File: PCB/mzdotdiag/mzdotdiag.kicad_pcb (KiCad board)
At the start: 2 copper layers, 58 parts, among them J1 Conn_01x25, J2 RST, J3 BOOT, J4 UART, Q1 Q_NPN_BEC, Q2 Q_NPN_BEC, Q3 Q_NPN_BEC, Q4 Q_NPN_BEC, Q5 Q_NPN_BEC, Q6 Q_NPN_BEC, Q7 Q_NPN_BEC, Q8 Q_NPN_BEC, Q9 Q_NPN_BEC, SW1 SW_Push, U1 4050, U3 ESP32-WROOM-32

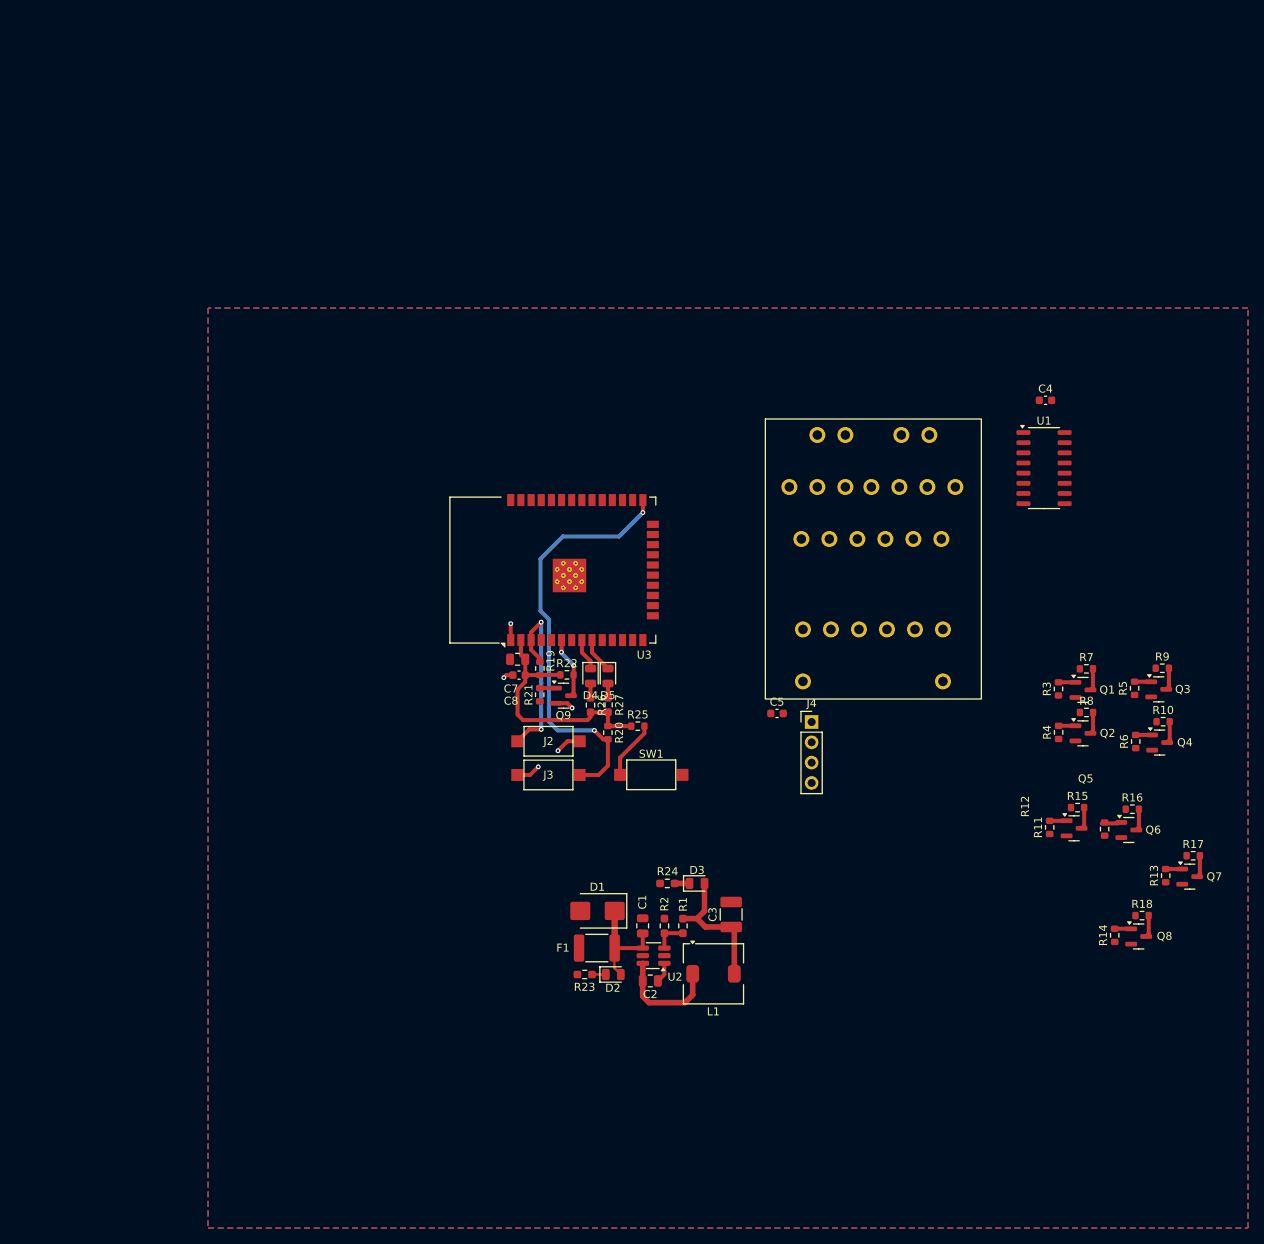
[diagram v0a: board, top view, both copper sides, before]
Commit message: schematic and pcb update with new levelshifter IC
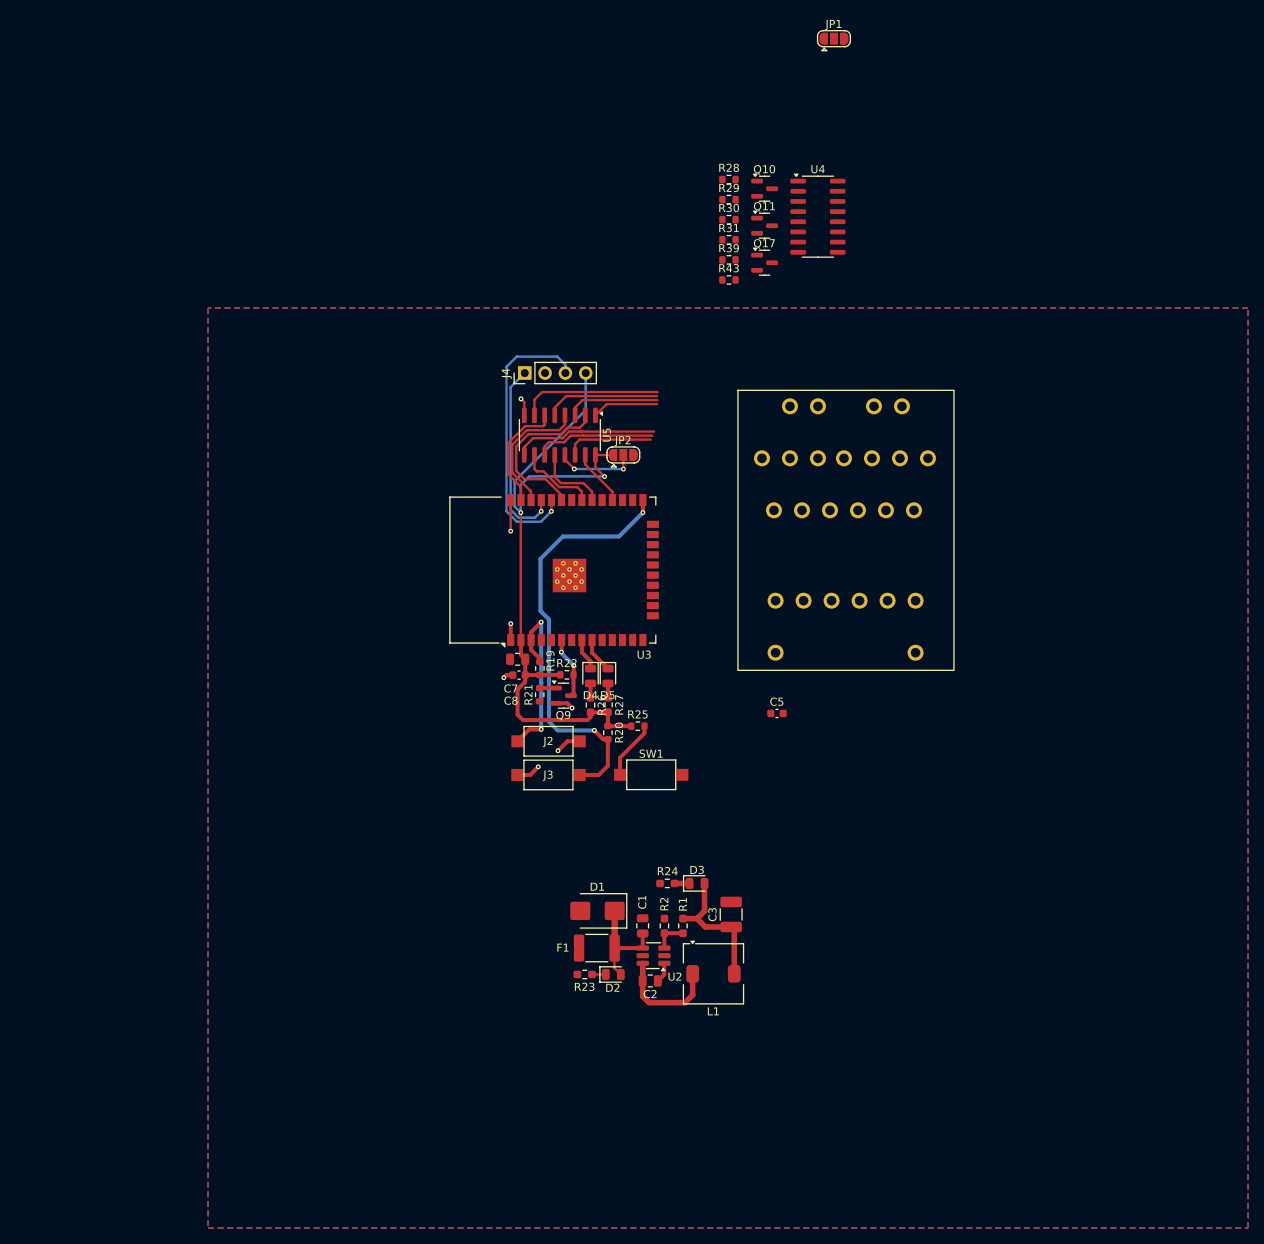
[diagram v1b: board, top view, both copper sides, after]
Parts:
- removed C4: 100nF, Capacitor_SMD:C_0603_1608Metric
- removed Q1, Q2, Q3, Q4, Q5, Q6, Q7, Q8: Q_NPN_BEC, Package_TO_SOT_SMD:SOT-23
- removed R10, R15, R16, R17, R18, R7, R8, R9: 10k, Resistor_SMD:R_0603_1608Metric
- removed R11, R12, R13, R14, R3, R4, R5, R6: 1k, Resistor_SMD:R_0603_1608Metric
- removed U1: 4050, Package_SO:SO-16_3.9x9.9mm_P1.27mm
- added JP1: SolderJumper_3_Open, Jumper:SolderJumper-3_P1.3mm_Open_RoundedPad1.0x1.5mm, F.Cu at (128.2, 6.33)
- added JP2: SolderJumper_3_Open, Jumper:SolderJumper-3_P1.3mm_Open_RoundedPad1.0x1.5mm, F.Cu at (101.9, 58.4)
- added Q10: Q_NPN_BEC, Package_TO_SOT_SMD:SOT-23, F.Cu at (119.6, 25.1)
- added Q11: Q_NPN_BEC, Package_TO_SOT_SMD:SOT-23, F.Cu at (119.6, 29.7)
- added Q17: Q_NPN_BEC, Package_TO_SOT_SMD:SOT-23, F.Cu at (119.6, 34.3)
- added R28: 1k, Resistor_SMD:R_0603_1608Metric, F.Cu at (115.1, 23.9)
- added R29: 10k, Resistor_SMD:R_0603_1608Metric, F.Cu at (115.1, 26.4)
- added R30: 1k, Resistor_SMD:R_0603_1608Metric, F.Cu at (115.1, 29.0)
- added R31: 10k, Resistor_SMD:R_0603_1608Metric, F.Cu at (115.1, 31.5)
- added R39: 1k, Resistor_SMD:R_0603_1608Metric, F.Cu at (115.1, 34.0)
- added R43: 10k, Resistor_SMD:R_0603_1608Metric, F.Cu at (115.1, 36.5)
- added U4: MC14504B, Package_SO:SOIC-16_3.9x9.9mm_P1.27mm, F.Cu at (126.2, 28.6)
- added U5: MC14504B, Package_SO:SOIC-16_3.9x9.9mm_P1.27mm, F.Cu at (94.0, 55.9)
- moved J4 56.5 mm to (89.6, 48.1), turned to 90 degrees
- moved J1 4.96 mm to (129.5, 65.3)
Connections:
- U3 pad 10: /FAC3V3 -> unconnected-(U3-IO25-Pad10)
- U3 pad 11: /FAB3V3 -> unconnected-(U3-IO26-Pad11)
- U3 pad 12: /FSC3V3 -> unconnected-(U3-IO27-Pad12)
- U3 pad 13: /ESP32_TFA -> /ESP32_TAT
- U3 pad 14: /ESP32_TAT -> /ESP32_TFA
- U3 pad 28: /ESP32_TAC -> /FSC3V3
- U3 pad 30: /ESP32_TEN -> /FAB3V3
- U3 pad 31: /ESP32_TSC -> /FAC3V3
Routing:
- net /3.3V: track 48.7 -> 105.9 mm, vias 0 -> 2
- net Net-(J4-Pin_3): track 0.00 -> 35.5 mm, vias 0 -> 1
- net Net-(J4-Pin_1): track 0.00 -> 23.8 mm, vias 0 -> 1
- net /FEN3V3: track 0.00 -> 21.4 mm
- net /FAC: track 0.00 -> 18.0 mm
- net /FAT: track 0.00 -> 17.7 mm
- net /FBS3V3: track 0.00 -> 16.7 mm
- net /FAB: track 0.00 -> 15.1 mm
- net /FAT3V3: track 0.00 -> 14.5 mm
- net /FBS: track 0.00 -> 14.4 mm
- net /FEN: track 0.00 -> 11.6 mm
- net /FSC: track 0.00 -> 11.0 mm
- net Net-(JP2-C): track 0.00 -> 10.2 mm, vias 0 -> 2
- net /FAC3V3: track 0.00 -> 9.90 mm
- net /FAB3V3: track 0.00 -> 9.22 mm
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
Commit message: updates to PCB
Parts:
- moved JP1 34.5 mm to (138.7, 39.2)
- moved U4 31.6 mm to (114.9, 58.1), turned to 90 degrees
- moved R1 29.6 mm to (128.4, 94.6)
- moved R2 29.6 mm to (126.1, 94.6)
- moved R24 29.6 mm to (126.4, 89.3)
- moved D3 29.6 mm to (130.1, 89.3)
- moved L1 29.6 mm to (132.2, 100.6)
- moved U2 29.6 mm to (124.7, 98.3)
- moved C3 29.6 mm to (134.4, 93.2)
- moved D2 29.6 mm to (119.7, 100.7)
- moved F1 29.6 mm to (117.6, 97.4)
- moved C1 29.6 mm to (123.3, 94.6)
- moved C2 29.6 mm to (124.3, 101.5)
- moved D1 29.6 mm to (117.7, 92.7)
- moved R23 29.6 mm to (116.1, 100.7)
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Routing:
- net /3.3V: track 105.9 -> 171.1 mm
- net Net-(U3-IO5): track 7.34 -> 38.4 mm
- net /B+: track 8.31 -> 21.8 mm, vias 0 -> 2
- net GND: track 18.0 -> 20.1 mm, vias 7 -> 8
- net /FSC: track 11.0 -> 13.1 mm
- net /FAB: track 15.1 -> 16.9 mm
- net /FAC: track 18.0 -> 19.6 mm
- net Net-(J3-Pin_2): track 53.2 -> 52.1 mm
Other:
- board text added: "BOOT"
- board text added: "BTN1"
- board text added: "RST"

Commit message: pcb upd
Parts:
- moved J1 10.6 mm to (143.5, 64.6)
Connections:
- U3 pad 14: /ESP32_TFA -> /ESP32_TAB
- U3 pad 16: /ESP32_TBS -> /ESP32_TSC
- U3 pad 23: /ESP32_TAB -> /ESP32_TEN
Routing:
- net /ESP32_TAB: track 0.00 -> 30.9 mm
- net /ESP32_TSC: track 0.00 -> 23.9 mm
- net /TEN: track 0.00 -> 15.1 mm
- net /TSC: track 0.00 -> 12.3 mm
- net /ESP32_TEN: track 0.00 -> 12.2 mm
- net /ESP32_TAT: track 0.00 -> 12.0 mm
- net /TAB: track 0.00 -> 9.97 mm
- net /ESP32_TAC: track 0.00 -> 9.00 mm
- net /ESP32_TBS: track 0.00 -> 5.34 mm
- net Net-(J3-Pin_2): track 52.1 -> 55.3 mm
- net GND: track 20.1 -> 21.9 mm, vias 8 -> 9
- net /IG-: track 0.00 -> 1.19 mm, vias 0 -> 1
- net Net-(U3-IO5): track 38.4 -> 39.1 mm, vias 0 -> 2

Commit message: finished wiring
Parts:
- removed Q17: Q_NPN_BEC, Package_TO_SOT_SMD:SOT-23
- removed R39: 1k, Resistor_SMD:R_0603_1608Metric
- removed R43: 10k, Resistor_SMD:R_0603_1608Metric
- moved R28 44.2 mm to (111.2, 68.0)
- moved Q10 42.2 mm to (115.2, 67.0)
- moved Q11 41.3 mm to (115.1, 70.8)
- moved R30 41.1 mm to (111.2, 69.8)
- moved R29 40.5 mm to (118.3, 66.8), turned to 90 degrees
- moved R31 39.2 mm to (118.3, 70.6), turned to 90 degrees
- moved JP1 29.7 mm to (121.6, 63.5)
- moved D1 8.77 mm to (113.7, 84.9), turned to 90 degrees
- moved D2 8.22 mm to (114.9, 94.0)
- moved F1 8.22 mm to (112.8, 90.7)
- moved R1 8.22 mm to (123.6, 87.9)
- moved R2 8.22 mm to (121.3, 87.9)
- moved C1 8.22 mm to (118.5, 87.9)
- moved C2 8.22 mm to (119.5, 94.8)
- moved C3 8.22 mm to (129.6, 86.5)
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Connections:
- C1 pad 2: Net-(D1-K) -> /B+_PROT
- D1 pad 1: Net-(D1-K) -> /B+_PROT
- D2 pad 2: Net-(D1-K) -> /B+_PROT
- F1 pad 2: Net-(D1-K) -> /B+_PROT
- R29 pad 1: /B+ -> /B+_PROT
- R31 pad 1: /B+ -> /B+_PROT
- U2 pad 4: Net-(D1-K) -> /B+_PROT
- U2 pad 5: Net-(D1-K) -> /B+_PROT
- U3 pad 10: unconnected-(U3-IO25-Pad10) -> /ESP32_TFA
- U3 pad 11: unconnected-(U3-IO26-Pad11) -> /ESP32_TBS
- U3 pad 12: unconnected-(U3-IO27-Pad12) -> /ESP32_TAC
- U4 pad 16: /B+ -> /B+_PROT
- U5 pad 1: /B+ -> /B+_PROT
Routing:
- net /IG-: track 1.19 -> 90.5 mm, vias 1 -> 3
- net /B+_PROT: track 0.00 -> 88.6 mm, vias 0 -> 5
- net /B+: track 21.8 -> 82.9 mm, vias 2 -> 0
- net /FSC: track 13.1 -> 60.5 mm, vias 0 -> 2
- net /FAB: track 16.9 -> 62.4 mm, vias 0 -> 5
- net /FAC: track 19.6 -> 59.9 mm, vias 0 -> 2
- net /TAB: track 9.97 -> 50.2 mm
- net /FBS: track 14.4 -> 54.0 mm
- net /F/P: track 0.00 -> 39.4 mm
- net /TAC: track 0.00 -> 38.4 mm, vias 0 -> 1
- net /TBS: track 0.00 -> 35.7 mm, vias 0 -> 1
- net /FAT: track 17.7 -> 51.5 mm
- net /TFA: track 0.00 -> 32.4 mm
- net /FEN: track 11.6 -> 42.3 mm, vias 0 -> 1
- net /ESP32_TBS: track 5.34 -> 33.5 mm
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
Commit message: some graphical updates
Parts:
- added G***: LOGO, LOGO, F.Cu at (144.0, 95.8)
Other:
- board text added: "Professional MX-5 Diagnostics"

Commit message: order files and pcb done
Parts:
- moved C7 61.0 mm to (36.0, 53.1)
- moved D1 61.0 mm to (61.0, 54.1)
- moved D3 61.0 mm to (72.6, 51.8)
- moved J1 61.0 mm to (90.8, 33.9)
- moved D5 61.0 mm to (47.3, 55.2)
- moved Q11 61.0 mm to (62.4, 40.0)
- moved R25 61.0 mm to (51.0, 61.5)
- moved R27 61.0 mm to (47.3, 58.9)
- moved C1 61.0 mm to (65.8, 57.1)
- moved C2 61.0 mm to (66.8, 64.0)
- moved C5 61.0 mm to (51.0, 59.6)
- moved D2 61.0 mm to (62.2, 63.2)
- moved D4 61.0 mm to (45.1, 55.2)
- moved F1 61.0 mm to (60.1, 59.9)
- moved G*** 61.0 mm to (91.3, 65.0)
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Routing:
- net GND: vias 28 -> 50
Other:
- board outline added: 79.8 x 60.3 mm
- board text added: "3.3V"
